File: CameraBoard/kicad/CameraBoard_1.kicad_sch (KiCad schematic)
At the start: 61 parts, among them Q1 SI7465DP-T1-E3, U1 MP26124GR-Z, U2 TPS63070, U3 LM2678SD-12/NOPB

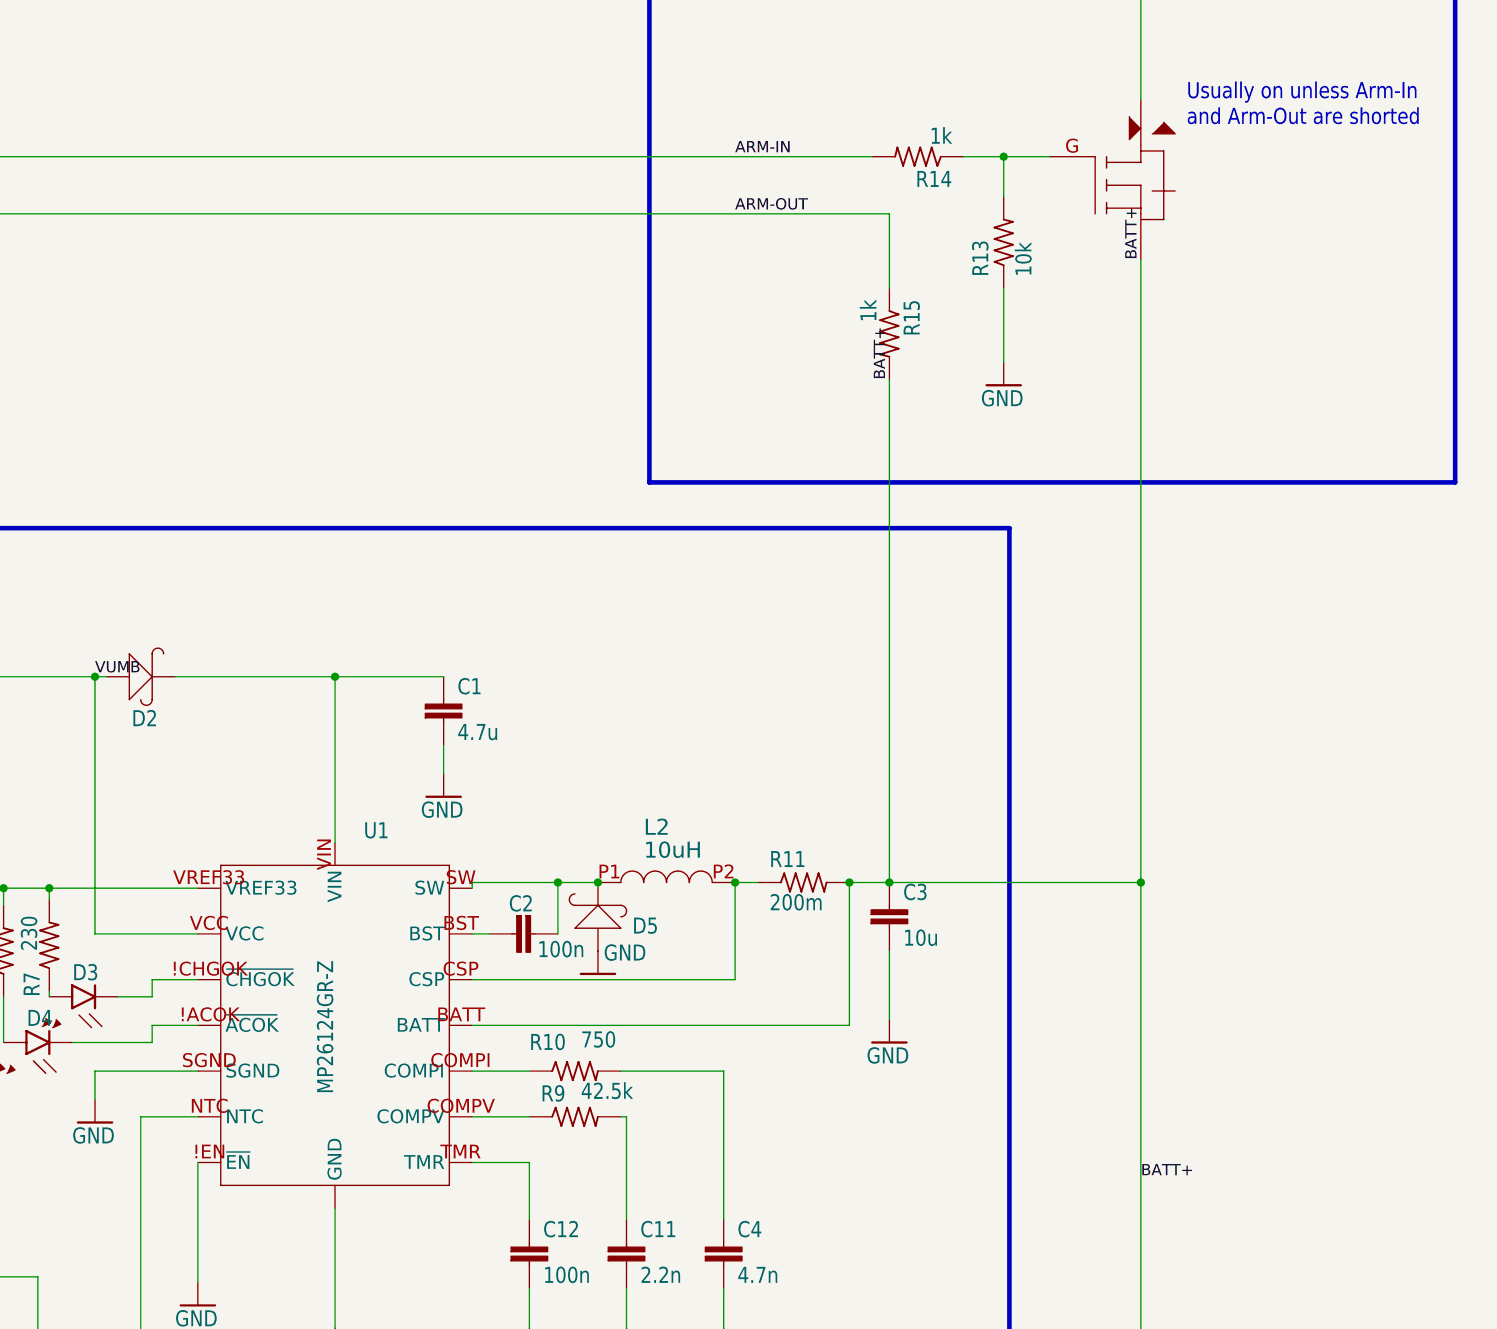
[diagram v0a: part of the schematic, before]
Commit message: Changed pulldown to 150k and added note about flipped connector.
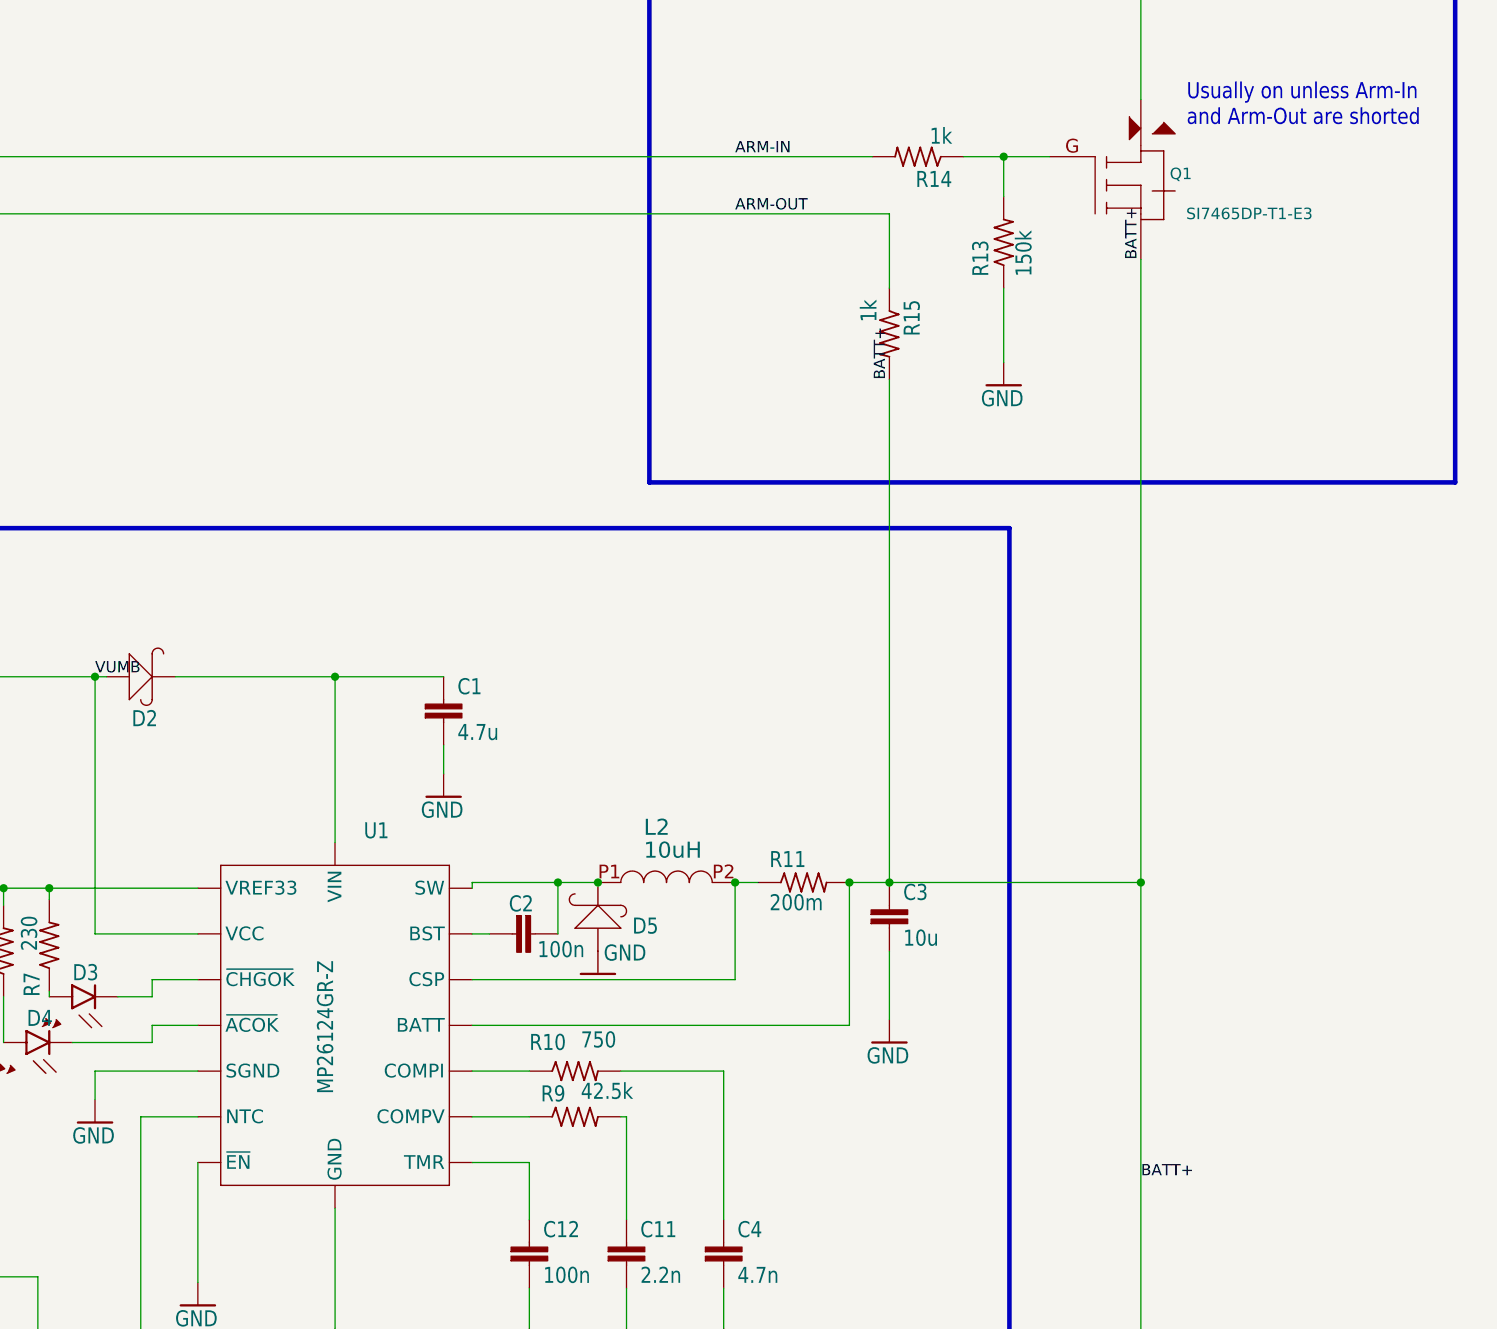
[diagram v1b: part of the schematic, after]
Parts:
- R13: value 10k -> 150k
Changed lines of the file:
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@@
 			)
 		)
-		(property "Value" "10k"
+		(property "Value" "150k"
 			(at 243.967 127 0)
 			(effects
@@
 		(dnp no)
 		(property "Reference" "Q1"
-			(at 250.825 113.665 0)
+			(at 260.35 115.57 0)
 			(effects
 				(font
 					(size 1.27 1.27)
 				)
-				(hide yes)
 			)
 		)
 		(property "Value" "SI7465DP-T1-E3"
-			(at 250.825 113.665 0)
+			(at 267.97 120.015 0)
 			(effects
 				(font
 					(size 1.27 1.27)
 				)
-				(hide yes)
 			)
 		)
@@
 			)
 		)
-		(property "Datasheet" ""
+		(property "Datasheet" "https://www.monolithicpower.com/en/documentview/productdocument/index/version/2/document_type/Datasheet/lang/en/sku/MP26124/document_id/3740"
 			(at 166.37 207.645 0)
 			(effects

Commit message: Cleaned up second page - fixed optoisolator symbols, added notes about levels and times, and cleaned up alot. Put in notes about mod wires.
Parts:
- removed JP10: PINHD-1X3, CameraBoard:1X03, symbol CameraBoard-eagle-import:PINHD-1X3
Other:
- note added: "OMG THERE'S NO UMB GND PIN!?!?! USE THERMISTOR'S INSTEAD"
- note removed: "Power to ATV Transmitter"
- moved on the sheet: C1, C11, C12, C14, C15, C18, C19, C2, C20, C21, C3, C4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

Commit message: Make schematic better, mostly cleaning up EAGLE import errors
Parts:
- D1: value SML-D12U1WT86 -> GRN
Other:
- note added: "12V @ 5A Max"
- note added: "16.8V @ 1A Max"
- note added: "4S Battery Pack"
- note added: "4S LiPo Charger"
- note added: "5V @ 2A Max"
- note added: "ARM + TELEMETRUM + VUMB"
- note added: "Note: will charge battery even if arming switch is off"
- note removed: "Battery"
- note removed: "Incoming signals VUMB - 19V"
- note removed: "LED to indicate power is on"
- note removed: "LiPo Charger"
- note removed: "Output: 12V, 5A Max"
- note removed: "Output: 16.8V, 1A Max"
- note removed: "Output: 5V, 2A Max"
- moved on the sheet: C10, C14, C15, C16, C17, C18, C19, C20, C21, C28, C5, C6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

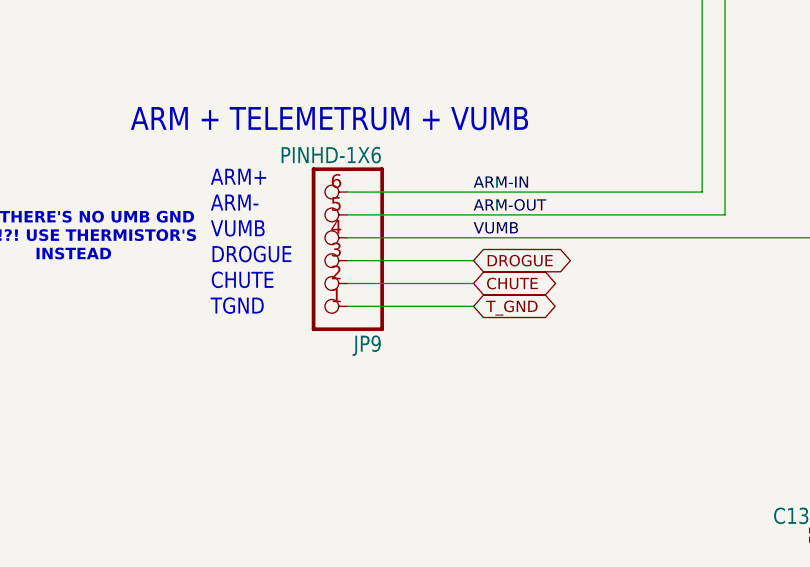
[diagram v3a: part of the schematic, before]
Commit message: replaced the timer logic for a d flip flop
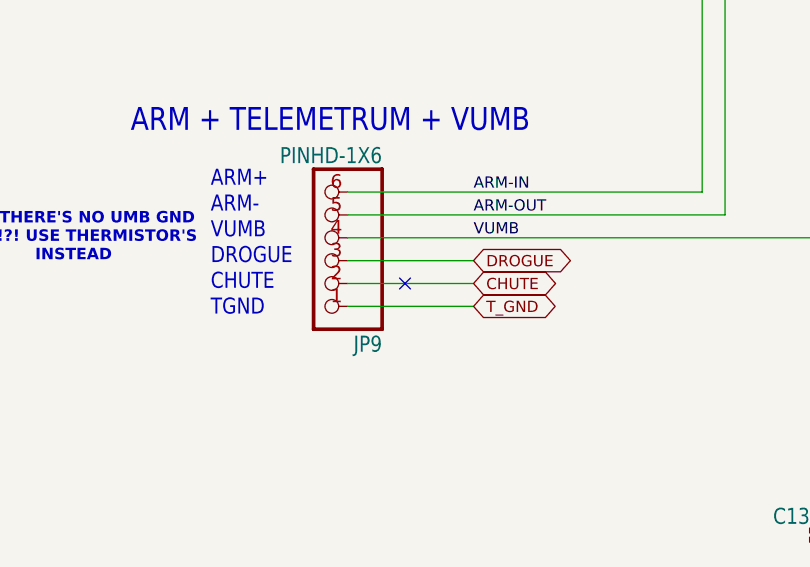
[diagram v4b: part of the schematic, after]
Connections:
- no-connect marks 0 -> 1
